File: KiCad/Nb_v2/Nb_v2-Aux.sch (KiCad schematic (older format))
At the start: 45 parts, among them K1 PWR SEL, P10 CONN_1, P11 CONN_1, P13 ISP, P20 CONN_2, P24 DIL6, P25 DIL6, P26 DIL6, P27 DIL6, P28 DIL6, P29 DIL6, P30 DIL6, P31 DIL6, P32 DIL6, P33 DIL6, P34 DIL6, P35 DIL6, P36 DIL6, P37 DIL6, P41 STACK-L, P42 STACK-R, P49 CONN_1, P50 CONN_1, P51 CONN_1, P52 CONN_1, P7 FTDI, P8 CONN_1, P9 CONN_1, U6 DS1307, U9 78L05, X2 CRYSTAL

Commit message: Nb_v2 : schematic and Board updates
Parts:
- U9: footprint (none) -> Volt_Reg_78xx_Vert
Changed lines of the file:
@@
-EESchema Schematic File Version 2  date 1/28/2012 6:18:02 PM
+EESchema Schematic File Version 2  date 2/3/2012 6:08:16 PM
 LIBS:Nb_v2
 LIBS:power
@@
 Sheet 2 2
 Title "NachBau - WordClock"
-Date "28 jan 2012"
+Date "3 feb 2012"
 Rev "A"
 Comp ""
@@
 F 0 "U9" H 3900 3954 60  0000 C CNN
 F 1 "78L05" H 3750 4350 60  0000 C CNN
+F 2 "Volt_Reg_78xx_Vert" H 3750 4450 60  0001 C CNN
 	1    3750 4150
 	1    0    0    -1
@@
 $EndComp
 $Comp
-L GND #PWR26
+L GND #PWR018
 U 1 1 4ECE864C
 P 7250 5250
-F 0 "#PWR26" H 7250 5250 30  0001 C CNN
+F 0 "#PWR018" H 7250 5250 30  0001 C CNN
 F 1 "GND" H 7250 5180 30  0001 C CNN
 	1    7250 5250
@@
 $EndComp
 $Comp
-L VCC #PWR25
+L VCC #PWR019
 U 1 1 4ECE863E
 P 7250 3750
-F 0 "#PWR25" H 7250 3850 30  0001 C CNN
+F 0 "#PWR019" H 7250 3850 30  0001 C CNN
 F 1 "VCC" H 7250 3850 30  0000 C CNN
 	1    7250 3750
@@
 VCC
 $Comp
-L GND #PWR24
+L GND #PWR020
 U 1 1 4DBAC297
 P 4675 3025
-F 0 "#PWR24" H 4675 3025 30  0001 C CNN
+F 0 "#PWR020" H 4675 3025 30  0001 C CNN
 F 1 "GND" H 4675 2955 30  0001 C CNN
 	1    4675 3025
@@
 $EndComp
 $Comp
-L VCC #PWR23
+L VCC #PWR021
 U 1 1 4DBAC28D
 P 4675 825
-F 0 "#PWR23" H 4675 925 30  0001 C CNN
+F 0 "#PWR021" H 4675 925 30  0001 C CNN
 F 1 "VCC" H 4675 925 30  0000 C CNN
 	1    4675 825
@@
 $EndComp
 $Comp
-L GND #PWR21
+L GND #PWR022
 U 1 1 4C9A49B0
 P 3350 7250
-F 0 "#PWR21" H 3350 7250 30  0001 C CNN
+F 0 "#PWR022" H 3350 7250 30  0001 C CNN
 F 1 "GND" H 3350 7180 30  0001 C CNN
 	1    3350 7250
@@
 $EndComp
 $Comp
-L VCC #PWR22
+L VCC #PWR023
 U 1 1 4C9A4991
 P 4150 5750
-F 0 "#PWR22" H 4150 5850 30  0001 C CNN
+F 0 "#PWR023" H 4150 5850 30  0001 C CNN
 F 1 "VCC" H 4150 5850 30  0000 C CNN
 	1    4150 5750
@@
 $EndComp
 $Comp
-L VCC #PWR27
+L VCC #PWR024
 U 1 1 4C109AAB
 P 9400 1150
-F 0 "#PWR27" H 9400 1250 30  0001 C CNN
+F 0 "#PWR024" H 9400 1250 30  0001 C CNN
 F 1 "VCC" H 9400 1250 30  0000 C CNN
 	1    9400 1150
@@
 $EndComp
 $Comp
-L GND #PWR28
+L GND #PWR025
 U 1 1 4C109AAA
 P 9450 2350
-F 0 "#PWR28" H 9450 2350 30  0001 C CNN
+F 0 "#PWR025" H 9450 2350 30  0001 C CNN
 F 1 "GND" H 9450 2280 30  0001 C CNN
 	1    9450 2350
@@
 USB5V
 $Comp
-L VDD #PWR29
+L VDD #PWR026
 U 1 1 4C109AA4
 P 9600 1150
-F 0 "#PWR29" H 9600 1250 30  0001 C CNN
+F 0 "#PWR026" H 9600 1250 30  0001 C CNN
 F 1 "VDD" H 9600 1260 30  0000 C CNN
 	1    9600 1150
@@
 $EndComp
 $Comp
-L VSS #PWR20
+L VSS #PWR027
 U 1 1 4B3F12CE
 P 3050 5300
-F 0 "#PWR20" H 3050 5300 30  0001 C CNN
+F 0 "#PWR027" H 3050 5300 30  0001 C CNN
 F 1 "VSS" H 3150 5350 30  0000 C CNN
 	1    3050 5300
@@
 $EndComp
 $Comp
-L GND #PWR19
+L GND #PWR028
 U 1 1 4B3F12CB
 P 2600 5300
-F 0 "#PWR19" H 2600 5300 30  0001 C CNN
+F 0 "#PWR028" H 2600 5300 30  0001 C CNN
 F 1 "GND" H 2600 5230 30  0001 C CNN
 F 4 "GND" H 2500 5350 60  0000 C CNN "Field1"

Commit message: Nb_v2 updates from Christians feedback
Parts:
- removed X2: CRYSTAL, XTAL_2, symbol CRYSTAL
- added X2: CRYSTAL_2, symbol CRYSTAL_2
- renumbered D128 to D3, D129 to D4, R27 to R31
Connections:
- wire segments 207 -> 205
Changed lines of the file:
@@
-EESchema Schematic File Version 2  date 2/3/2012 6:08:16 PM
+EESchema Schematic File Version 2  date 2/9/2012 3:43:46 PM
 LIBS:Nb_v2
 LIBS:power
+LIBS:conn
 LIBS:Nb_v2-cache
 EELAYER 25  0
@@
 Sheet 2 2
 Title "NachBau - WordClock"
-Date "3 feb 2012"
+Date "9 feb 2012"
 Rev "A"
 Comp ""
@@
 Comment4 ""
 $EndDescr
+$Comp
+L CRYSTAL_2 X2
+U 1 1 4F338811
+P 4325 1900
+F 0 "X2" H 4325 2050 60  0000 C CNN
+F 1 "CRYSTAL_2" H 4325 1750 60  0000 C CNN
+	1    4325 1900
+	0    1    1    0
+$EndComp
 Text Label 5125 3600 0    40   ~ 0
 VIN
@@
 Wire Wire Line
 	7250 3900 7250 3750
-Connection ~ 3750 2900
-Wire Wire Line
-	3750 2900 3750 1900
-Wire Wire Line
-	3750 1900 4075 1900
 Wire Wire Line
 	4600 2000 4600 2250
@@
 3V3
 $Comp
-L DIODESCH D129
+L DIODESCH D4
 U 1 1 4ECE872F
 P 7250 4825
-F 0 "D129" H 7250 4925 40  0000 C CNN
+F 0 "D4" H 7250 4925 40  0000 C CNN
 F 1 "3V3_Z" H 7250 4725 40  0000 C CNN
 F 2 "diode_do35" H 7250 4825 60  0001 C CNN
@@
 $EndComp
 $Comp
-L GND #PWR018
+L GND #PWR017
 U 1 1 4ECE864C
 P 7250 5250
-F 0 "#PWR018" H 7250 5250 30  0001 C CNN
+F 0 "#PWR017" H 7250 5250 30  0001 C CNN
 F 1 "GND" H 7250 5180 30  0001 C CNN
 	1    7250 5250
@@
 $EndComp
 $Comp
-L VCC #PWR019
+L VCC #PWR018
 U 1 1 4ECE863E
 P 7250 3750
-F 0 "#PWR019" H 7250 3850 30  0001 C CNN
+F 0 "#PWR018" H 7250 3850 30  0001 C CNN
 F 1 "VCC" H 7250 3850 30  0000 C CNN
 	1    7250 3750
@@
 Text HLabel 6450 2000 2    40   Input ~ 0
 SQW
-$Comp
-L CRYSTAL X2
-U 1 1 4ECE81EB
-P 4325 1900
-F 0 "X2" H 4400 1750 60  0000 C CNN
-F 1 "CRYSTAL" H 4325 2075 60  0000 C CNN
-F 2 "XTAL_2" H 4325 1900 60  0001 C CNN
-	1    4325 1900
-	0    1    1    0
-$EndComp
 $Comp
 L DS1307 U6
@@
 VCC
 $Comp
-L GND #PWR020
+L GND #PWR019
 U 1 1 4DBAC297
 P 4675 3025
-F 0 "#PWR020" H 4675 3025 30  0001 C CNN
+F 0 "#PWR019" H 4675 3025 30  0001 C CNN
 F 1 "GND" H 4675 2955 30  0001 C CNN
 	1    4675 3025
@@
 $EndComp
 $Comp
-L VCC #PWR021
+L VCC #PWR020
 U 1 1 4DBAC28D
 P 4675 825
-F 0 "#PWR021" H 4675 925 30  0001 C CNN
+F 0 "#PWR020" H 4675 925 30  0001 C CNN
 F 1 "VCC" H 4675 925 30  0000 C CNN
 	1    4675 825
@@
 $EndComp
 $Comp
-L GND #PWR022
+L GND #PWR021
 U 1 1 4C9A49B0
 P 3350 7250
-F 0 "#PWR022" H 3350 7250 30  0001 C CNN
+F 0 "#PWR021" H 3350 7250 30  0001 C CNN
 F 1 "GND" H 3350 7180 30  0001 C CNN
 	1    3350 7250
@@
 $EndComp
 $Comp
-L VCC #PWR023
+L VCC #PWR022
 U 1 1 4C9A4991
 P 4150 5750
-F 0 "#PWR023" H 4150 5850 30  0001 C CNN
+F 0 "#PWR022" H 4150 5850 30  0001 C CNN
 F 1 "VCC" H 4150 5850 30  0000 C CNN
 	1    4150 5750
@@
 $EndComp
 $Comp
-L VCC #PWR024
+L VCC #PWR023
 U 1 1 4C109AAB
 P 9400 1150
-F 0 "#PWR024" H 9400 1250 30  0001 C CNN
+F 0 "#PWR023" H 9400 1250 30  0001 C CNN
 F 1 "VCC" H 9400 1250 30  0000 C CNN
 	1    9400 1150
@@
 $EndComp
 $Comp
-L GND #PWR025
+L GND #PWR024
 U 1 1 4C109AAA
 P 9450 2350
-F 0 "#PWR025" H 9450 2350 30  0001 C CNN
+F 0 "#PWR024" H 9450 2350 30  0001 C CNN
 F 1 "GND" H 9450 2280 30  0001 C CNN
 	1    9450 2350
@@
 USB5V
 $Comp
-L VDD #PWR026
+L VDD #PWR025
 U 1 1 4C109AA4
 P 9600 1150
-F 0 "#PWR026" H 9600 1250 30  0001 C CNN
+F 0 "#PWR025" H 9600 1250 30  0001 C CNN
 F 1 "VDD" H 9600 1260 30  0000 C CNN
 	1    9600 1150
@@
 $EndComp
 $Comp
-L VSS #PWR027
+L VSS #PWR026
 U 1 1 4B3F12CE
 P 3050 5300
-F 0 "#PWR027" H 3050 5300 30  0001 C CNN
+F 0 "#PWR026" H 3050 5300 30  0001 C CNN
 F 1 "VSS" H 3150 5350 30  0000 C CNN
 	1    3050 5300
@@
 $EndComp
 $Comp
-L GND #PWR028
+L GND #PWR027
 U 1 1 4B3F12CB
 P 2600 5300
-F 0 "#PWR028" H 2600 5300 30  0001 C CNN
+F 0 "#PWR027" H 2600 5300 30  0001 C CNN
 F 1 "GND" H 2600 5230 30  0001 C CNN
 F 4 "GND" H 2500 5350 60  0000 C CNN "Field1"
@@
 $EndComp
 $Comp
-L LED D128
+L LED D3
 U 1 1 4B3F12CA
 P 3050 4950
-F 0 "D128" H 3050 5050 50  0000 C CNN
+F 0 "D3" H 3050 5050 50  0000 C CNN
 F 1 "PWR" H 3050 4850 50  0000 C CNN
 F 2 "led_5mm_blue" H 3050 4950 60  0001 C CNN
@@
 $EndComp
 $Comp
-L R R27
+L R R31
 U 1 1 4B3F12C9
 P 3050 4450
-F 0 "R27" V 3130 4450 50  0000 C CNN
+F 0 "R31" V 3130 4450 50  0000 C CNN
 F 1 "1k" V 3050 4450 50  0000 C CNN
 F 2 "rc03_vert" H 3050 4450 60  0001 C CNN

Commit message: Nachbau updates to SCH and PCB
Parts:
- removed X2: CRYSTAL_2, symbol CRYSTAL_2
- added X2: CRYSTAL, XTAL_3, symbol CRYSTAL
- P20: value CONN_2 -> DC_IN
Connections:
- wire segments 205 -> 207

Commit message: Nb_v2 : added DS3231 to SCH and PCB. Not yet started on track layout
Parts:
- added P2: SDA, symbol CONN_2
- added P3: SCL, symbol CONN_2
- added R32, R33: 10k, rc03_vert, symbol R
- added U10: DS3231N, symbol DS3231N
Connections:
- wire segments 207 -> 236
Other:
- note added: "Mounting holes for Nb_v2\n4 no, 3mm\naround the board"
- note removed: "Mounting holes for C3Jr\n8 holes around the board\nwith 3mm mounting hole\n4 holes at corners for Housing\n4 holes near LEDs for Baffle"
- moved on the sheet: C10, CD1, CD2, CD3, P24, P25, P26, P27, P28, P29, P30, P31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

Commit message: Nb_v2 track layout in progress
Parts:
- P2, P3: footprint (none) -> pin_strip_2
- U10: footprint (none) -> DS3231
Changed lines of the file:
@@
-EESchema Schematic File Version 2  date Sunday 12 February 2012 12:21:59 AM IST
+EESchema Schematic File Version 2  date 2/17/2012 6:16:40 PM
 LIBS:Nb_v2
 LIBS:power
@@
 Sheet 2 2
 Title "NachBau - WordClock"
-Date "11 feb 2012"
+Date "17 feb 2012"
 Rev "A"
 Comp ""
@@
 F 0 "P3" V 4575 2400 40  0000 C CNN
 F 1 "SCL" V 4675 2400 40  0000 C CNN
+F 2 "pin_strip_2" V 4775 2400 40  0001 C CNN
 	1    4625 2400
 	0    1    1    0
@@
 F 0 "P2" V 4575 1450 40  0000 C CNN
 F 1 "SDA" V 4675 1450 40  0000 C CNN
+F 2 "pin_strip_2" V 4775 1450 40  0001 C CNN
 	1    4625 1450
 	0    -1   -1   0
@@
 F 0 "U10" H 6325 2350 60  0000 C CNN
 F 1 "DS3231N" H 5725 1400 60  0000 C CNN
+F 2 "DS3231" H 5725 1500 60  0001 C CNN
 	1    6025 1800
 	1    0    0    -1

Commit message: Nb_v2 : almost wrapped up. Some final touches to legend required.
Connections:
- net labels added: SCL_INT, SDA_INT
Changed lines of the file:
@@
-EESchema Schematic File Version 2  date Sunday 19 February 2012 09:05:15 PM IST
+EESchema Schematic File Version 2  date Tuesday 21 February 2012 01:53:29 AM IST
 LIBS:Nb_v2
 LIBS:power
@@
 Sheet 2 2
 Title "NachBau - WordClock"
-Date "19 feb 2012"
+Date "20 feb 2012"
 Rev "A"
 Comp ""
@@
 Comment4 ""
 $EndDescr
+Text Label 4800 2000 0    40   ~ 0
+SCL_INT
+Text Label 4800 1850 0    40   ~ 0
+SDA_INT
 Connection ~ 4875 5000
 Wire Wire Line

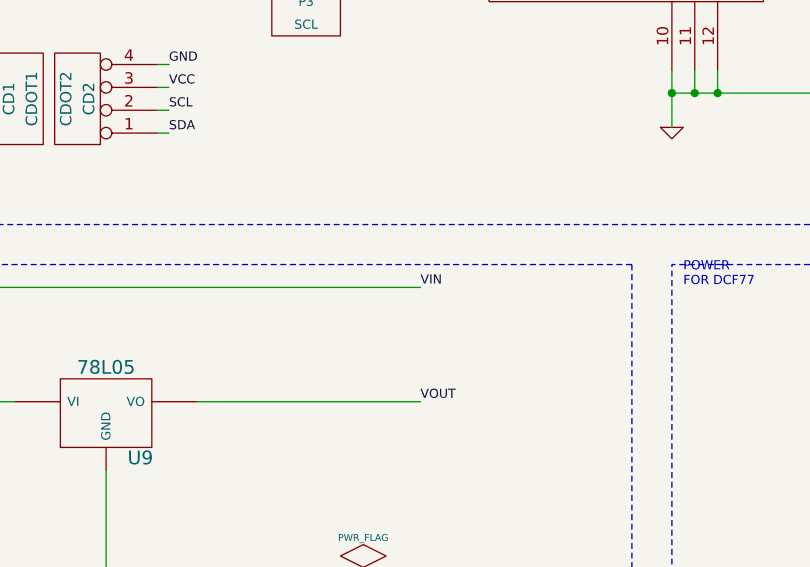
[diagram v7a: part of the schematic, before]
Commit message: Nb_v2 : added LED Voltage selector, Logos on Legend layer
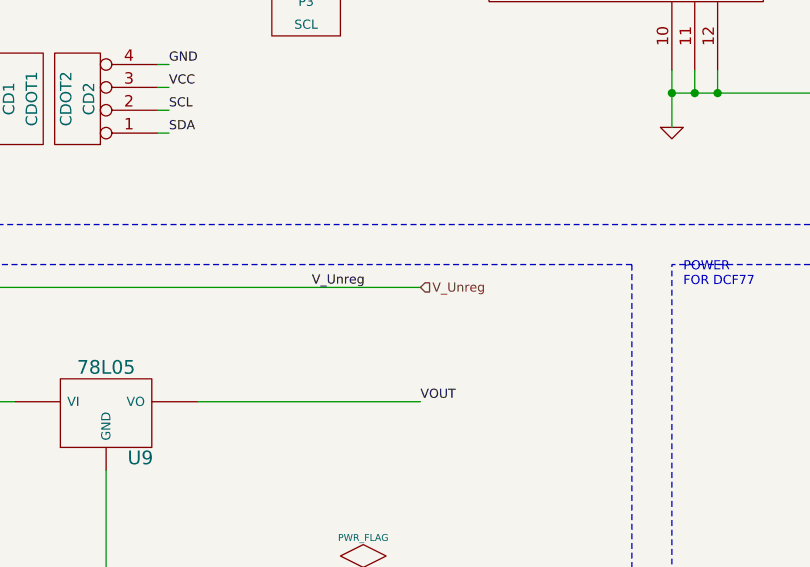
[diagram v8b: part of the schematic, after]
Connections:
- net labels added: V_Unreg
- net labels removed: VIN
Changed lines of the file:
@@
-EESchema Schematic File Version 2  date Tuesday 21 February 2012 01:53:29 AM IST
+EESchema Schematic File Version 2  date Tuesday 21 February 2012 09:46:58 PM IST
 LIBS:Nb_v2
 LIBS:power
@@
 Sheet 2 2
 Title "NachBau - WordClock"
-Date "20 feb 2012"
+Date "21 feb 2012"
 Rev "A"
 Comp ""
@@
 Comment4 ""
 $EndDescr
+Text HLabel 5125 3600 2    40   Input ~ 0
+V_Unreg
 Text Label 4800 2000 0    40   ~ 0
 SCL_INT
@@
 Connection ~ 975  1050
 $Comp
-L PWR_FLAG #FLG017
+L PWR_FLAG #FLG3
 U 1 1 4F36B85A
 P 4875 4925
-F 0 "#FLG017" H 4875 5195 30  0001 C CNN
+F 0 "#FLG3" H 4875 5195 30  0001 C CNN
 F 1 "PWR_FLAG" H 4875 5155 30  0000 C CNN
 	1    4875 4925
@@
 $EndComp
 $Comp
-L PWR_FLAG #FLG018
+L PWR_FLAG #FLG2
 U 1 1 4F36B823
 P 975 1025
-F 0 "#FLG018" H 975 1295 30  0001 C CNN
+F 0 "#FLG2" H 975 1295 30  0001 C CNN
 F 1 "PWR_FLAG" H 975 1255 30  0000 C CNN
 	1    975  1025
@@
 $EndComp
 $Comp
-L GND #PWR019
+L GND #PWR22
 U 1 1 4F36B419
 P 6225 2900
-F 0 "#PWR019" H 6225 2900 30  0001 C CNN
+F 0 "#PWR22" H 6225 2900 30  0001 C CNN
 F 1 "GND" H 6225 2830 30  0001 C CNN
 	1    6225 2900
@@
 	0    1    1    0
 $EndComp
-Text Label 5125 3600 0    40   ~ 0
-VIN
+Text Label 4650 3600 0    40   ~ 0
+V_Unreg
 $Comp
 L 78L05 U9
@@
 $EndComp
 $Comp
-L GND #PWR020
+L GND #PWR24
 U 1 1 4ECE864C
 P 7250 5250
-F 0 "#PWR020" H 7250 5250 30  0001 C CNN
+F 0 "#PWR24" H 7250 5250 30  0001 C CNN
 F 1 "GND" H 7250 5180 30  0001 C CNN
 	1    7250 5250
@@
 $EndComp
 $Comp
-L VCC #PWR021
+L VCC #PWR23
 U 1 1 4ECE863E
 P 7250 3750
-F 0 "#PWR021" H 7250 3850 30  0001 C CNN
+F 0 "#PWR23" H 7250 3850 30  0001 C CNN
 F 1 "VCC" H 7250 3850 30  0000 C CNN
 	1    7250 3750
@@
 VCC
 $Comp
-L GND #PWR022
+L GND #PWR17
 U 1 1 4DBAC297
 P 2050 3025
-F 0 "#PWR022" H 2050 3025 30  0001 C CNN
+F 0 "#PWR17" H 2050 3025 30  0001 C CNN
 F 1 "GND" H 2050 2955 30  0001 C CNN
 	1    2050 3025
@@
 $EndComp
 $Comp
-L VCC #PWR023
+L VCC #PWR16
 U 1 1 4DBAC28D
 P 2050 825
-F 0 "#PWR023" H 2050 925 30  0001 C CNN
+F 0 "#PWR16" H 2050 925 30  0001 C CNN
 F 1 "VCC" H 2050 925 30  0000 C CNN
 	1    2050 825
@@
 $EndComp
 $Comp
-L GND #PWR024
+L GND #PWR20
 U 1 1 4C9A49B0
 P 4000 7250
-F 0 "#PWR024" H 4000 7250 30  0001 C CNN
+F 0 "#PWR20" H 4000 7250 30  0001 C CNN
 F 1 "GND" H 4000 7180 30  0001 C CNN
 	1    4000 7250
@@
 $EndComp
 $Comp
-L VCC #PWR025
+L VCC #PWR21
 U 1 1 4C9A4991
 P 4800 5750
-F 0 "#PWR025" H 4800 5850 30  0001 C CNN
+F 0 "#PWR21" H 4800 5850 30  0001 C CNN
 F 1 "VCC" H 4800 5850 30  0000 C CNN
 	1    4800 5750
@@
 $EndComp
 $Comp
-L VCC #PWR026
+L VCC #PWR25
 U 1 1 4C109AAB
 P 9400 1150
-F 0 "#PWR026" H 9400 1250 30  0001 C CNN
+F 0 "#PWR25" H 9400 1250 30  0001 C CNN
 F 1 "VCC" H 9400 1250 30  0000 C CNN
 	1    9400 1150
@@
 $EndComp
 $Comp
-L GND #PWR027
+L GND #PWR26
 U 1 1 4C109AAA
 P 9450 2350
-F 0 "#PWR027" H 9450 2350 30  0001 C CNN
+F 0 "#PWR26" H 9450 2350 30  0001 C CNN
 F 1 "GND" H 9450 2280 30  0001 C CNN
 	1    9450 2350
@@
 USB5V
 $Comp
-L VDD #PWR028
+L VDD #PWR27
 U 1 1 4C109AA4
 P 9600 1150
-F 0 "#PWR028" H 9600 1250 30  0001 C CNN
+F 0 "#PWR27" H 9600 1250 30  0001 C CNN
 F 1 "VDD" H 9600 1260 30  0000 C CNN
 	1    9600 1150
@@
 $EndComp
 $Comp
-L VSS #PWR029
+L VSS #PWR19
 U 1 1 4B3F12CE
 P 3050 5300
-F 0 "#PWR029" H 3050 5300 30  0001 C CNN
+F 0 "#PWR19" H 3050 5300 30  0001 C CNN
 F 1 "VSS" H 3150 5350 30  0000 C CNN
 	1    3050 5300
@@
 $EndComp
 $Comp
-L GND #PWR030
+L GND #PWR18
 U 1 1 4B3F12CB
 P 2600 5300
-F 0 "#PWR030" H 2600 5300 30  0001 C CNN
+F 0 "#PWR18" H 2600 5300 30  0001 C CNN
 F 1 "GND" H 2600 5230 30  0001 C CNN
 F 4 "GND" H 2500 5350 60  0000 C CNN "Field1"
